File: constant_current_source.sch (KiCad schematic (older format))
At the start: 19 parts

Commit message: Add datasheet and footprint to LT3474
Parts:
- U?: footprint (none) -> Package_SO:TSSOP-16-1EP_4.4x5mm_P0.65mm
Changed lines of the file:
@@
 F 0 "U?" H 5350 3675 50  0000 C CNN
 F 1 "LT3474" H 5350 3584 50  0000 C CNN
-F 2 "" H 5350 3100 50  0001 C CNN
-F 3 "" H 5350 3100 50  0001 C CNN
+F 2 "Package_SO:TSSOP-16-1EP_4.4x5mm_P0.65mm" H 5350 3100 50  0001 C CNN
+F 3 "https://www.analog.com/media/en/technical-documentation/data-sheets/3474fd.pdf" H 5350 3100 50  0001 C CNN
 	1    5350 3050
 	1    0    0    -1

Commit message: Add PWM dimming
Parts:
- added C?: 100n, symbol Device:C
- added Q?: IRLML0030, symbol Device:Q_PMOS_GSD
- added R?: 10k, symbol Device:R
- C?: value 100n -> 3n3
- C?: value 2u2 16V -> 10u 16V
- C?: value 100n 16V -> 2u2 16V
- D?: value D_Schottky -> MBR0520L
- J?: value GND -> LED-
- J?: value LED -> LED+
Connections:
- wire segments 73 -> 81
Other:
- moved on the sheet: D?, J?, JP?, L?, R?

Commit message: Finish sheets
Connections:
- wire segments 81 -> 83
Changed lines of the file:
@@
 	4450 2700 4450 2400
 Wire Wire Line
-	4450 2400 3850 2400
+	4450 2400 4100 2400
 Wire Wire Line
 	3850 2400 3850 2450
@@
 Wire Wire Line
 	6000 2750 6300 2750
+$Comp
+L power:PWR_FLAG #FLG?
+U 1 1 604F43EE
+P 4100 2300
+F 0 "#FLG?" H 4100 2375 50  0001 C CNN
+F 1 "PWR_FLAG" H 4100 2473 50  0000 C CNN
+F 2 "" H 4100 2300 50  0001 C CNN
+F 3 "~" H 4100 2300 50  0001 C CNN
+	1    4100 2300
+	1    0    0    -1
+$EndComp
+Wire Wire Line
+	4100 2300 4100 2400
+Connection ~ 4100 2400
+Wire Wire Line
+	4100 2400 3850 2400
 $EndSCHEMATC

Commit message: Fix mosfet symbol
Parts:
- Q?: symbol Device:Q_PMOS_GSD -> Device:Q_NMOS_GSD
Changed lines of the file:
@@
 constant current source - buck converter
 $Comp
-L Device:Q_PMOS_GSD Q?
+L Device:Q_NMOS_GSD Q?
 U 1 1 6020B63A
 P 5750 3950

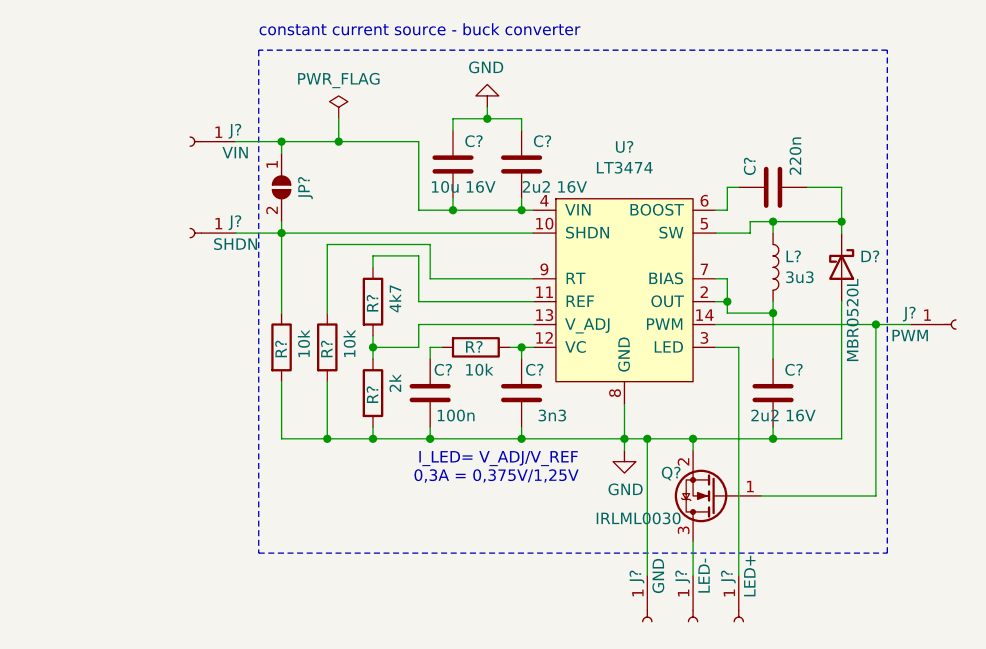
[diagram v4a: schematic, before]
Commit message: Annotate sheets and assign symbols
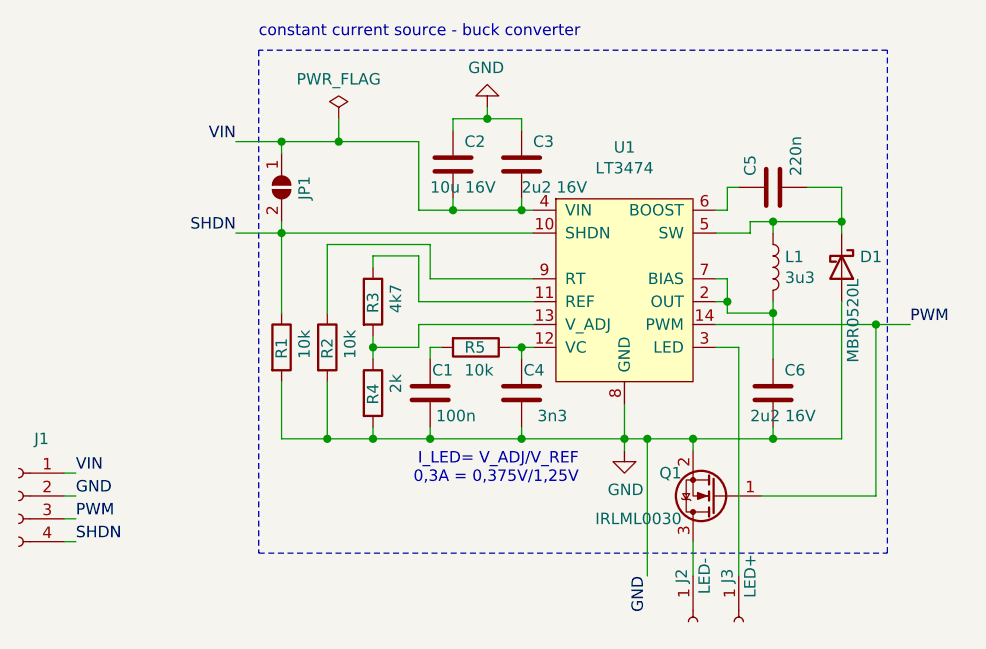
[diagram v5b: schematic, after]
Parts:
- removed J?: SHDN, symbol Connector:Conn_01x01_Female
- removed J?: VIN, symbol Connector:Conn_01x01_Female
- removed J?: PWM, symbol Connector:Conn_01x01_Female
- removed J?: GND, symbol Connector:Conn_01x01_Female
- added J1: Conn, Connector_Molex:Molex_PicoBlade_53047-0410_1x04_P1.25mm_Vertical, symbol Connector:Conn_01x04_Female
- C1, C3, C4, C5, C6: renamed from C?; footprint (none) -> Capacitor_SMD:C_0603_1608Metric
- C2: renamed from C?; footprint (none) -> Capacitor_SMD:C_0805_2012Metric
- D1: renamed from D?; footprint (none) -> Diode_SMD:D_SOD-123
- J2, J3: renamed from J?; footprint (none) -> Connector_PinHeader_2.54mm:PinHeader_1x01_P2.54mm_Vertical
- JP1: renamed from JP?; footprint (none) -> Jumper:SolderJumper-2_P1.3mm_Open_TrianglePad1.0x1.5mm
- L1: renamed from L?; footprint (none) -> Inductor_SMD:L_Abracon_ASPI-3012S
- Q1: renamed from Q?; footprint (none) -> Package_TO_SOT_SMD:SOT-23
- R1, R2, R3, R4, R5: renamed from R?; footprint (none) -> Resistor_SMD:R_0603_1608Metric
- gave numbers to parts that had none: 1
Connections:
- net GND: now also J1.2 (Pin_2)
- net SHDN: now reaches JP1.2 (B), R1.1, U1.10 (SHDN)
- net SHDN: now also J1.4 (Pin_4)
- net PWM: now reaches Q1.1 (G), U1.14 (PWM)
- net PWM: now also J1.3 (Pin_3)
- net VIN: now reaches C2.2, C3.2, JP1.1 (A), U1.4 (VIN)
- net VIN: now also J1.1 (Pin_1)
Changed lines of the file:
@@
 $EndDescr
 $Comp
-L extraSymbols:LT3474 U?
+L extraSymbols:LT3474 U1
 U 1 1 601DBDCB
 P 5350 3050
-F 0 "U?" H 5350 3675 50  0000 C CNN
+F 0 "U1" H 5350 3675 50  0000 C CNN
 F 1 "LT3474" H 5350 3584 50  0000 C CNN
 F 2 "Package_SO:TSSOP-16-1EP_4.4x5mm_P0.65mm" H 5350 3100 50  0001 C CNN
@@
 $EndComp
 $Comp
-L power:GND #PWR?
+L power:GND #PWR02
 U 1 1 601DD2F4
 P 5350 3750
-F 0 "#PWR?" H 5350 3500 50  0001 C CNN
+F 0 "#PWR02" H 5350 3500 50  0001 C CNN
 F 1 "GND" H 5355 3577 50  0000 C CNN
 F 2 "" H 5350 3750 50  0001 C CNN
@@
 	5350 3750 5350 3700
 $Comp
-L Device:C C?
+L Device:C C4
 U 1 1 601DD8D8
 P 4900 3500
-F 0 "C?" H 5000 3400 50  0000 R CNN
+F 0 "C4" H 5000 3400 50  0000 R CNN
 F 1 "3n3" H 5100 3600 50  0000 R CNN
-F 2 "" H 4938 3350 50  0001 C CNN
+F 2 "Capacitor_SMD:C_0603_1608Metric" H 4938 3350 50  0001 C CNN
 F 3 "~" H 4900 3500 50  0001 C CNN
 	1    4900 3500
@@
 	4250 3300 4450 3300
 $Comp
-L Device:R R?
+L Device:R R4
 U 1 1 601DF467
 P 4250 3500
-F 0 "R?" V 4250 3450 50  0000 L CNN
+F 0 "R4" V 4250 3450 50  0000 L CNN
 F 1 "2k" V 4350 3500 50  0000 L CNN
-F 2 "" V 4180 3500 50  0001 C CNN
+F 2 "Resistor_SMD:R_0603_1608Metric" V 4180 3500 50  0001 C CNN
 F 3 "~" H 4250 3500 50  0001 C CNN
 	1    4250 3500
@@
 	4250 3700 4500 3700
 $Comp
-L Device:R R?
+L Device:R R3
 U 1 1 601DEB7E
 P 4250 3100
-F 0 "R?" V 4250 3050 50  0000 L CNN
+F 0 "R3" V 4250 3050 50  0000 L CNN
 F 1 "4k7" V 4350 3050 50  0000 L CNN
-F 2 "" V 4180 3100 50  0001 C CNN
+F 2 "Resistor_SMD:R_0603_1608Metric" V 4180 3100 50  0001 C CNN
 F 3 "~" H 4250 3100 50  0001 C CNN
 	1    4250 3100
@@
 Text Notes 5150 3900 2    50   ~ 0
 I_LED= V_ADJ/V_REF\n0,3A = 0,375V/1,25V
-$Comp
-L Connector:Conn_01x01_Female J?
-U 1 1 601E5ECF
-P 3450 2800
-F 0 "J?" H 3250 2750 50  0000 C CNN
-F 1 "SHDN" H 3250 2850 50  0000 C CNN
-F 2 "" H 3450 2800 50  0001 C CNN
-F 3 "~" H 3450 2800 50  0001 C CNN
-	1    3450 2800
-	-1   0    0    1
-$EndComp
 Wire Wire Line
 	4950 2800 3850 2800
@@
 Connection ~ 4250 3700
 $Comp
-L Jumper:SolderJumper_2_Open JP?
+L Jumper:SolderJumper_2_Open JP1
 U 1 1 601EC0F6
 P 3850 2600
-F 0 "JP?" H 3800 2700 50  0000 L CNN
+F 0 "JP1" H 3800 2700 50  0000 L CNN
 F 1 "SolderJumper_2_Open" V 3895 2668 50  0001 L CNN
-F 2 "" H 3850 2600 50  0001 C CNN
+F 2 "Jumper:SolderJumper-2_P1.3mm_Open_TrianglePad1.0x1.5mm" H 3850 2600 50  0001 C CNN
 F 3 "~" H 3850 2600 50  0001 C CNN
 	1    3850 2600
@@
 Wire Wire Line
 	3850 2400 3850 2450
-$Comp
-L Connector:Conn_01x01_Female J?
-U 1 1 601ED7C4
-P 3450 2400
-F 0 "J?" H 3250 2350 50  0000 C CNN
-F 1 "VIN" H 3250 2450 50  0000 C CNN
-F 2 "" H 3450 2400 50  0001 C CNN
-F 3 "~" H 3450 2400 50  0001 C CNN
-	1    3450 2400
-	-1   0    0    1
-$EndComp
 Connection ~ 3850 2400
 Wire Wire Line
 	3650 2400 3850 2400
 $Comp
-L Device:C C?
+L Device:C C2
 U 1 1 601F2317
 P 4600 2500
-F 0 "C?" H 4650 2600 50  0000 L CNN
+F 0 "C2" H 4650 2600 50  0000 L CNN
 F 1 "10u 16V" H 4500 2400 50  0000 L CNN
-F 2 "" H 4638 2350 50  0001 C CNN
+F 2 "Capacitor_SMD:C_0805_2012Metric" H 4638 2350 50  0001 C CNN
 F 3 "~" H 4600 2500 50  0001 C CNN
 	1    4600 2500
@@
 $EndComp
 $Comp
-L Device:C C?
+L Device:C C3
 U 1 1 601F2971
 P 4900 2500
-F 0 "C?" H 4950 2600 50  0000 L CNN
+F 0 "C3" H 4950 2600 50  0000 L CNN
 F 1 "2u2 16V" H 4900 2400 50  0000 L CNN
-F 2 "" H 4938 2350 50  0001 C CNN
+F 2 "Capacitor_SMD:C_0603_1608Metric" H 4938 2350 50  0001 C CNN
 F 3 "~" H 4900 2500 50  0001 C CNN
 	1    4900 2500
@@
 	4600 2700 4450 2700
 $Comp
-L power:GND #PWR?
+L power:GND #PWR01
 U 1 1 601F37F5
 P 4750 2250
-F 0 "#PWR?" H 4750 2000 50  0001 C CNN
+F 0 "#PWR01" H 4750 2000 50  0001 C CNN
 F 1 "GND" H 4755 2077 50  0000 C CNN
 F 2 "" H 4750 2250 50  0001 C CNN
@@
 	4750 2300 4600 2300
 $Comp
-L Device:R R?
+L Device:R R1
 U 1 1 601FB2F4
 P 3850 3300
-F 0 "R?" V 3850 3250 50  0000 L CNN
+F 0 "R1" V 3850 3250 50  0000 L CNN
 F 1 "10k" V 3950 3250 50  0000 L CNN
-F 2 "" V 3780 3300 50  0001 C CNN
+F 2 "Resistor_SMD:R_0603_1608Metric" V 3780 3300 50  0001 C CNN
 F 3 "~" H 3850 3300 50  0001 C CNN
 	1    3850 3300
@@
 $EndComp
 $Comp
-L Device:R R?
+L Device:R R2
 U 1 1 601FB781
 P 4050 3300
-F 0 "R?" V 4050 3250 50  0000 L CNN
+F 0 "R2" V 4050 3250 50  0000 L CNN
 F 1 "10k" V 4150 3250 50  0000 L CNN
-F 2 "" V 3980 3300 50  0001 C CNN
+F 2 "Resistor_SMD:R_0603_1608Metric" V 3980 3300 50  0001 C CNN
 F 3 "~" H 4050 3300 50  0001 C CNN
 	1    4050 3300
@@
 Wire Wire Line
 	4050 3700 4250 3700
-$Comp
-L Connector:Conn_01x01_Female J?
-U 1 1 60202E06
-P 6800 3200
-F 0 "J?" H 6600 3150 50  0000 C CNN
-F 1 "PWM" H 6600 3250 50  0000 C CNN
-F 2 "" H 6800 3200 50  0001 C CNN
-F 3 "~" H 6800 3200 50  0001 C CNN
-	1    6800 3200
-	1    0    0    1
-$EndComp
 Wire Wire Line
 	6600 3200 6450 3200
@@
 	5800 3100 5750 3100
 $Comp
-L Device:L L?
+L Device:L L1
 U 1 1 6020600C
 P 6000 2950
-F 0 "L?" H 6052 2996 50  0000 L CNN
+F 0 "L1" H 6052 2996 50  0000 L CNN
 F 1 "3u3" H 6052 2905 50  0000 L CNN
-F 2 "" H 6000 2950 50  0001 C CNN
+F 2 "Inductor_SMD:L_Abracon_ASPI-3012S" H 6000 2950 50  0001 C CNN
 F 3 "~" H 6000 2950 50  0001 C CNN
 	1    6000 2950
@@
 $EndComp
 $Comp
-L Device:D_Schottky D?
+L Device:D_Schottky D1
 U 1 1 60206A7E
 P 6300 2950
-F 0 "D?" V 6254 3030 50  0000 L CNN
+F 0 "D1" V 6254 3030 50  0000 L CNN
 F 1 "MBR0520L" H 6350 3000 50  0000 L CNN
-F 2 "" H 6300 2950 50  0001 C CNN
+F 2 "Diode_SMD:D_SOD-123" H 6300 2950 50  0001 C CNN
 F 3 "~" H 6300 2950 50  0001 C CNN
 	1    6300 2950
@@
 $EndComp
 $Comp
-L Device:C C?
+L Device:C C6
 U 1 1 60208B4A
 P 6000 3500
-F 0 "C?" H 6050 3600 50  0000 L CNN
+F 0 "C6" H 6050 3600 50  0000 L CNN
 F 1 "2u2 16V" H 5900 3400 50  0000 L CNN
-F 2 "" H 6038 3350 50  0001 C CNN
+F 2 "Capacitor_SMD:C_0603_1608Metric" H 6038 3350 50  0001 C CNN
 F 3 "~" H 6000 3500 50  0001 C CNN
 	1    6000 3500
@@
 Connection ~ 6000 3700
 $Comp
-L Device:C C?
+L Device:C C5
 U 1 1 602178A4
 P 6000 2600
-F 0 "C?" H 6050 2700 50  0000 L CNN
+F 0 "C5" H 6050 2700 50  0000 L CNN
 F 1 "220n" H 6050 2500 50  0000 L CNN
-F 2 "" H 6038 2450 50  0001 C CNN
+F 2 "Capacitor_SMD:C_0603_1608Metric" H 6038 2450 50  0001 C CNN
 F 3 "~" H 6000 2600 50  0001 C CNN
 	1    6000 2600
@@
 Wire Notes Line
 	3750 2000 3750 4200
-$Comp
-L Connector:Conn_01x01_Female J?
-U 1 1 602218C3
-P 5450 4500
-F 0 "J?" H 5250 4450 50  0000 C CNN
-F 1 "GND" H 5250 4550 50  0000 C CNN
-F 2 "" H 5450 4500 50  0001 C CNN
-F 3 "~" H 5450 4500 50  0001 C CNN
-	1    5450 4500
-	0    1    1    0
-$EndComp
 Wire Wire Line
 	5450 4300 5450 3700
@@
 	5450 3700 5350 3700
 $Comp
-L Connector:Conn_01x01_Female J?
+L Connector:Conn_01x01_Female J2
 U 1 1 6022D25C
 P 5650 4500
-F 0 "J?" H 5450 4450 50  0000 C CNN
+F 0 "J2" H 5450 4450 50  0000 C CNN
 F 1 "LED-" H 5450 4550 50  0000 C CNN
-F 2 "" H 5650 4500 50  0001 C CNN
+F 2 "Connector_PinHeader_2.54mm:PinHeader_1x01_P2.54mm_Vertical" H 5650 4500 50  0001 C CNN
 F 3 "~" H 5650 4500 50  0001 C CNN
 	1    5650 4500
@@
 $EndComp
 $Comp
-L Connector:Conn_01x01_Female J?
+L Connector:Conn_01x01_Female J3
 U 1 1 6022D62E
 P 5850 4500
-F 0 "J?" H 5650 4450 50  0000 C CNN
+F 0 "J3" H 5650 4450 50  0000 C CNN
 F 1 "LED+" H 5650 4550 50  0000 C CNN
-F 2 "" H 5850 4500 50  0001 C CNN
+F 2 "Connector_PinHeader_2.54mm:PinHeader_1x01_P2.54mm_Vertical" H 5850 4500 50  0001 C CNN
 F 3 "~" H 5850 4500 50  0001 C CNN
 	1    5850 4500
@@
 constant current source - buck converter
 $Comp
-L Device:Q_NMOS_GSD Q?
+L Device:Q_NMOS_GSD Q1
 U 1 1 6020B63A
 P 5750 3950
-F 0 "Q?" H 5900 3850 50  0000 L CNN
+F 0 "Q1" H 5900 3850 50  0000 L CNN
 F 1 "IRLML0030" H 5900 4050 50  0000 L CNN
-F 2 "" H 5950 4050 50  0001 C CNN
+F 2 "Package_TO_SOT_SMD:SOT-23" H 5950 4050 50  0001 C CNN
 F 3 "~" H 5750 3950 50  0001 C CNN
 	1    5750 3950
@@
 	6450 3200 5750 3200
 $Comp
-L Device:C C?
+L Device:C C1
 U 1 1 602251E7
 P 4500 3500
-F 0 "C?" H 4600 3400 50  0000 R CNN
+F 0 "C1" H 4600 3400 50  0000 R CNN
 F 1 "100n" H 4700 3600 50  0000 R CNN
-F 2 "" H 4538 3350 50  0001 C CNN
+F 2 "Capacitor_SMD:C_0603_1608Metric" H 4538 3350 50  0001 C CNN
 F 3 "~" H 4500 3500 50  0001 C CNN
 	1    4500 3500
@@
 $EndComp
 $Comp
-L Device:R R?
+L Device:R R5
 U 1 1 60225806
 P 4700 3300
-F 0 "R?" V 4700 3250 50  0000 L CNN
+F 0 "R5" V 4700 3250 50  0000 L CNN
 F 1 "10k" V 4800 3250 50  0000 L CNN
-F 2 "" V 4630 3300 50  0001 C CNN
+F 2 "Resistor_SMD:R_0603_1608Metric" V 4630 3300 50  0001 C CNN
 F 3 "~" H 4700 3300 50  0001 C CNN
 	1    4700 3300
@@
 	6000 2750 6300 2750
 $Comp
-L power:PWR_FLAG #FLG?
+L power:PWR_FLAG #FLG01
 U 1 1 604F43EE
 P 4100 2300
-F 0 "#FLG?" H 4100 2375 50  0001 C CNN
+F 0 "#FLG01" H 4100 2375 50  0001 C CNN
 F 1 "PWR_FLAG" H 4100 2473 50  0000 C CNN
 F 2 "" H 4100 2300 50  0001 C CNN
@@
 Wire Wire Line
 	4100 2400 3850 2400
+$Comp
+L Connector:Conn_01x04_Female J1
+U 1 1 603C6B34
+P 2700 3950
+F 0 "J1" H 2600 4200 50  0000 C CNN
+F 1 "Conn" H 2500 4000 50  0001 C CNN
+F 2 "Connector_Molex:Molex_PicoBlade_53047-0410_1x04_P1.25mm_Vertical" H 2700 3950 50  0001 C CNN
+F 3 "~" H 2700 3950 50  0001 C CNN
+	1    2700 3950
+	-1   0    0    -1
+$EndComp
+Text Label 3650 2400 2    50   ~ 0
+VIN
+Text Label 3650 2800 2    50   ~ 0
+SHDN
+Text Label 6600 3200 0    50   ~ 0
+PWM
+Text Label 5450 4300 3    50   ~ 0
+GND
+Text Label 2950 3950 0    50   ~ 0
+GND
+Text Label 2950 4150 0    50   ~ 0
+SHDN
+Text Label 2950 3850 0    50   ~ 0
+VIN
+Text Label 2950 4050 0    50   ~ 0
+PWM
+Wire Wire Line
+	2950 4050 2900 4050
+Wire Wire Line
+	2950 4150 2900 4150
+Wire Wire Line
+	2900 3950 2950 3950
+Wire Wire Line
+	2950 3850 2900 3850
 $EndSCHEMATC
